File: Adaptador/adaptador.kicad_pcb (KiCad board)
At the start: 2 copper layers, 3 parts, among them P1 CONN_02X06, P2 CONN_01X03, U1 MCP3002

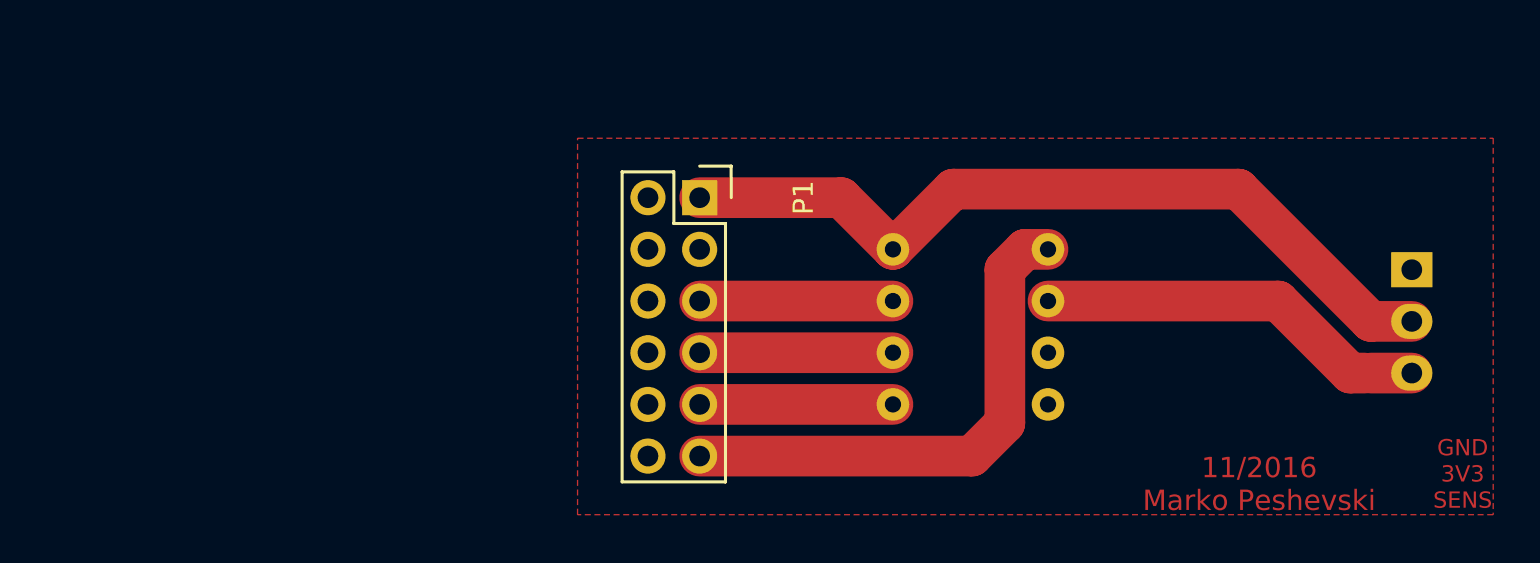
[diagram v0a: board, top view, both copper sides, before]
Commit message: Canvis a la PCB. No puc dormir sino. Crec que ara esta be (el coure queda a la vista cap a dalt i tot es munta per baix
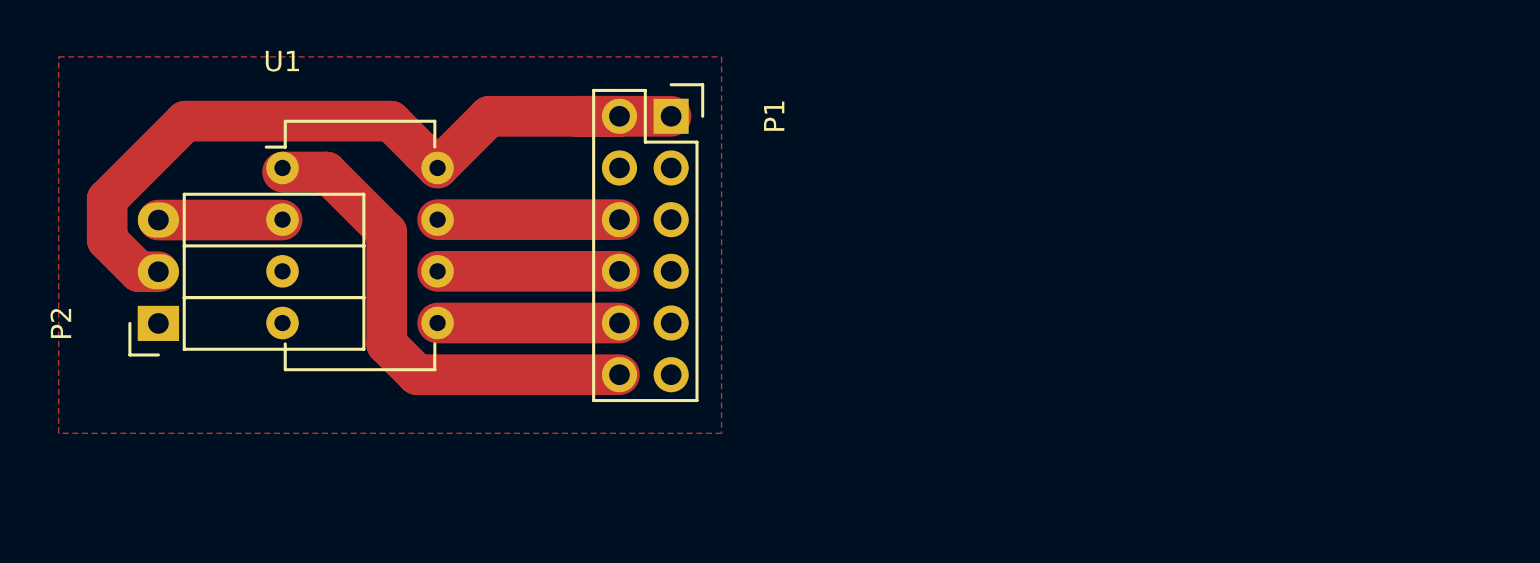
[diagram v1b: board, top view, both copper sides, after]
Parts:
- P2, U1: moved to F.Cu
- moved P2 61.7 mm to (148.2, 103.1), turned to 90 degrees
- moved U1 37.8 mm to (154.3, 95.5), turned to 0 degrees
- moved P1 4.24 mm to (173.4, 92.9)
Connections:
- P1 pad 10: Net-(P1-Pad10) -> /MOSI
- P1 pad 11: //CS -> Net-(P1-Pad11)
- P1 pad 12: Net-(P1-Pad12) -> //CS
- P1 pad 5: /SCK -> Net-(P1-Pad5)
- P1 pad 6: Net-(P1-Pad6) -> /SCK
- P1 pad 7: /MISO -> Net-(P1-Pad7)
- P1 pad 8: Net-(P1-Pad8) -> /MISO
- P1 pad 9: /MOSI -> Net-(P1-Pad9)
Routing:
- net /SENS: track 19.3 -> 6.11 mm
- net //CS: track 25.8 -> 23.9 mm
- net /3V3: track 40.0 -> 38.5 mm
- net /MOSI: track 9.56 -> 8.94 mm
- net /SCK: track 9.50 -> 8.94 mm
- net /MISO: track 9.50 -> 8.94 mm
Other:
- board text removed: "11/2016 Marko Peshevski"
- board text removed: "GND 3V3 SENS"
